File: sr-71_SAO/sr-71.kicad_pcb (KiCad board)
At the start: 2 copper layers, 81.4 x 39.2 mm, 10 parts, among them J1 Conn_02x03_Counter_Clockwise

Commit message: Working on the main village base badge
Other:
- net class Default removed

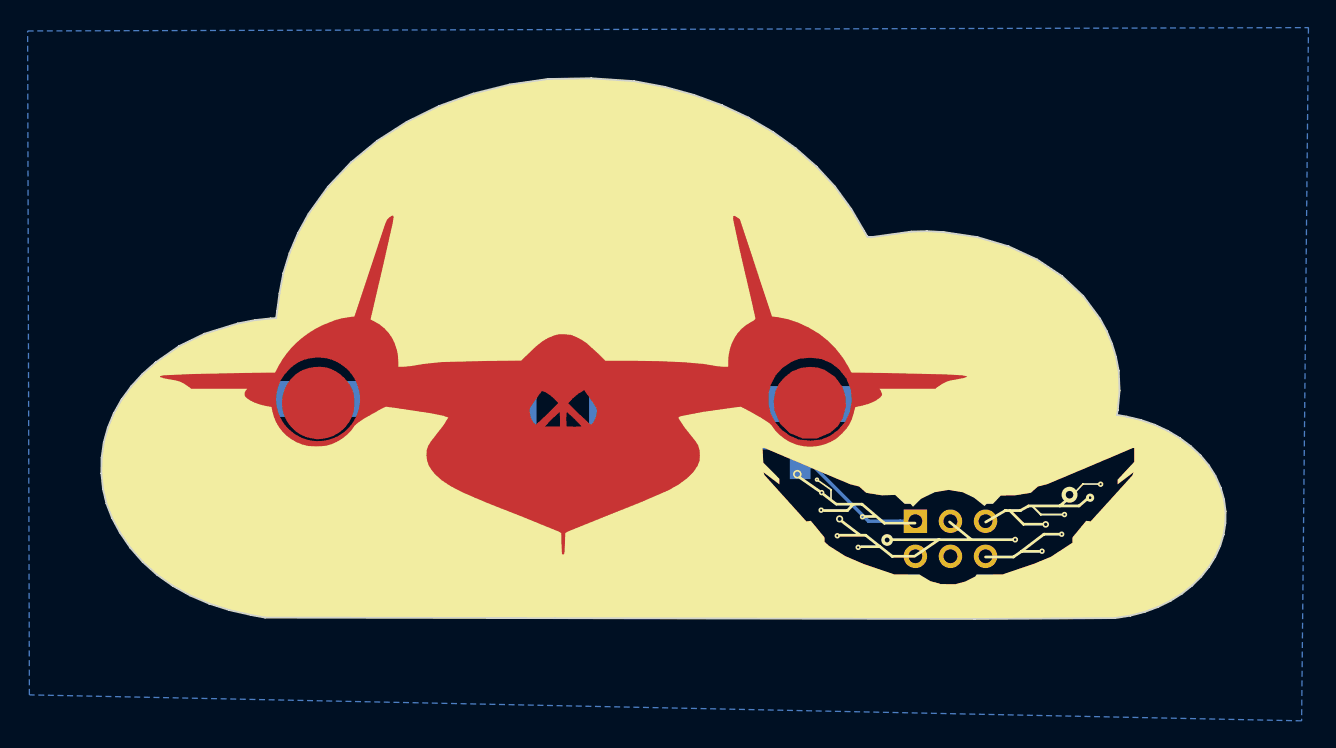
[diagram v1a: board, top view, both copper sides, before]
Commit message: adjustement to sr-71
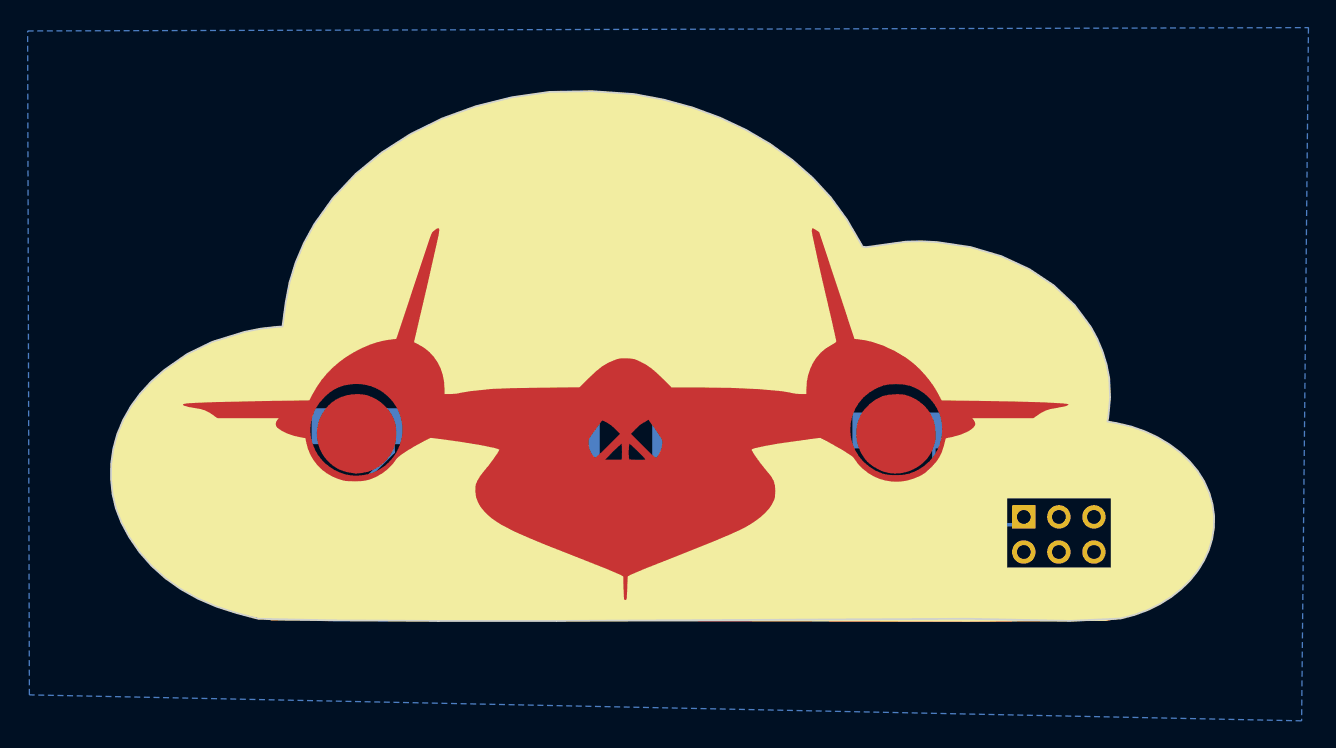
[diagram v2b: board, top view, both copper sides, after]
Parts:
- removed the svg2mod at (156.9, 100.1)
- added svg2mod: G***, sr-71:sr71_symetricView_smaller, F.Cu at (155.8, 101.9)
- moved J1 7.86 mm to (182.9, 112.3)
- moved D3 6.75 mm to (173.8, 106.0)
- moved R2 6.11 mm to (154.2, 112.1)
- moved R3 5.98 mm to (173.7, 111.6)
- moved D2 5.02 mm to (154.1, 106.7)
- moved D1 3.62 mm to (134.7, 105.7), turned to 0 degrees
- moved R1 2.61 mm to (135.1, 111.6)
- moved svg2mod 2.34 mm to (180.3, 100.3)
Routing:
- net Net-(D1-Pad2): track 12.3 -> 7.53 mm
- net Net-(D3-Pad2): track 8.19 -> 5.97 mm
- net Net-(D2-Pad2): track 5.77 -> 7.16 mm
- net VCC: track 90.1 -> 91.4 mm
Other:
- board size 81.4 x 39.2 mm -> 79.9 x 38.4 mm
- rule pad_to_mask_clearance: 0.051 -> 0
- board text added: "V04 @cybertestpilot"
- board text removed: "V03"
